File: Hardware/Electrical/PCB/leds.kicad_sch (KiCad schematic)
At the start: 0 parts

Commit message: battery charger added
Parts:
- added U7: TMP1075DSG, Package_SON:WSON-8-1EP_2x2mm_P0.5mm_EP0.9x1.6mm, symbol Sensor_Temperature:TMP1075DSG
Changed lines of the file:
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@@
 	(generator_version "9.0")
 	(paper "A4")
+	(symbol
+		(lib_id "Sensor_Temperature:TMP1075DSG")
+		(at 224.79 101.6 0)
+		(unit 1)
+		(exclude_from_sim no)
+		(in_bom yes)
+		(on_board yes)
+		(dnp no)
+		(fields_autoplaced yes)
+		(property "Reference" "U7"
+			(at 226.9333 91.44 0)
+			(effects
+				(font
+					(size 1.27 1.27)
+				)
+				(justify left)
+			)
+		)
+		(property "Value" "TMP1075DSG"
+			(at 226.9333 93.98 0)
+			(effects
+				(font
+					(size 1.27 1.27)
+				)
+				(justify left)
+			)
+		)
+		(property "Footprint" "Package_SON:WSON-8-1EP_2x2mm_P0.5mm_EP0.9x1.6mm"
+			(at 226.695 107.95 0)
+			(effects
+				(font
+					(size 1.27 1.27)
+				)
+				(hide yes)
+			)
+		)
+		(property "Datasheet" "https://www.ti.com/lit/gpn/tmp1075"
+			(at 224.79 101.6 0)
+			(effects
+				(font
+					(size 1.27 1.27)
+				)
+				(hide yes)
+			)
+		)
+		(property "Description" "I2C-bus digital temperature sensor and thermal watchdog, WSON-8"
+			(at 224.79 101.6 0)
+			(effects
+				(font
+					(size 1.27 1.27)
+				)
+				(hide yes)
+			)
+		)
+		(pin "3"
+		)
+		(pin "5"
+		)
+		(pin "6"
+		)
+		(pin "9"
+		)
+		(pin "2"
+		)
+		(pin "8"
+		)
+		(pin "1"
+		)
+		(pin "4"
+		)
+		(pin "7"
+		)
+		(instances
+			(project ""
+				(path "/8e3abcc5-43e9-4b34-9640-a0acd90473e7/255c8fde-d8cc-4a06-ba23-cdcfa512cf28"
+					(reference "U7")
+					(unit 1)
+				)
+			)
+		)
+	)
 )

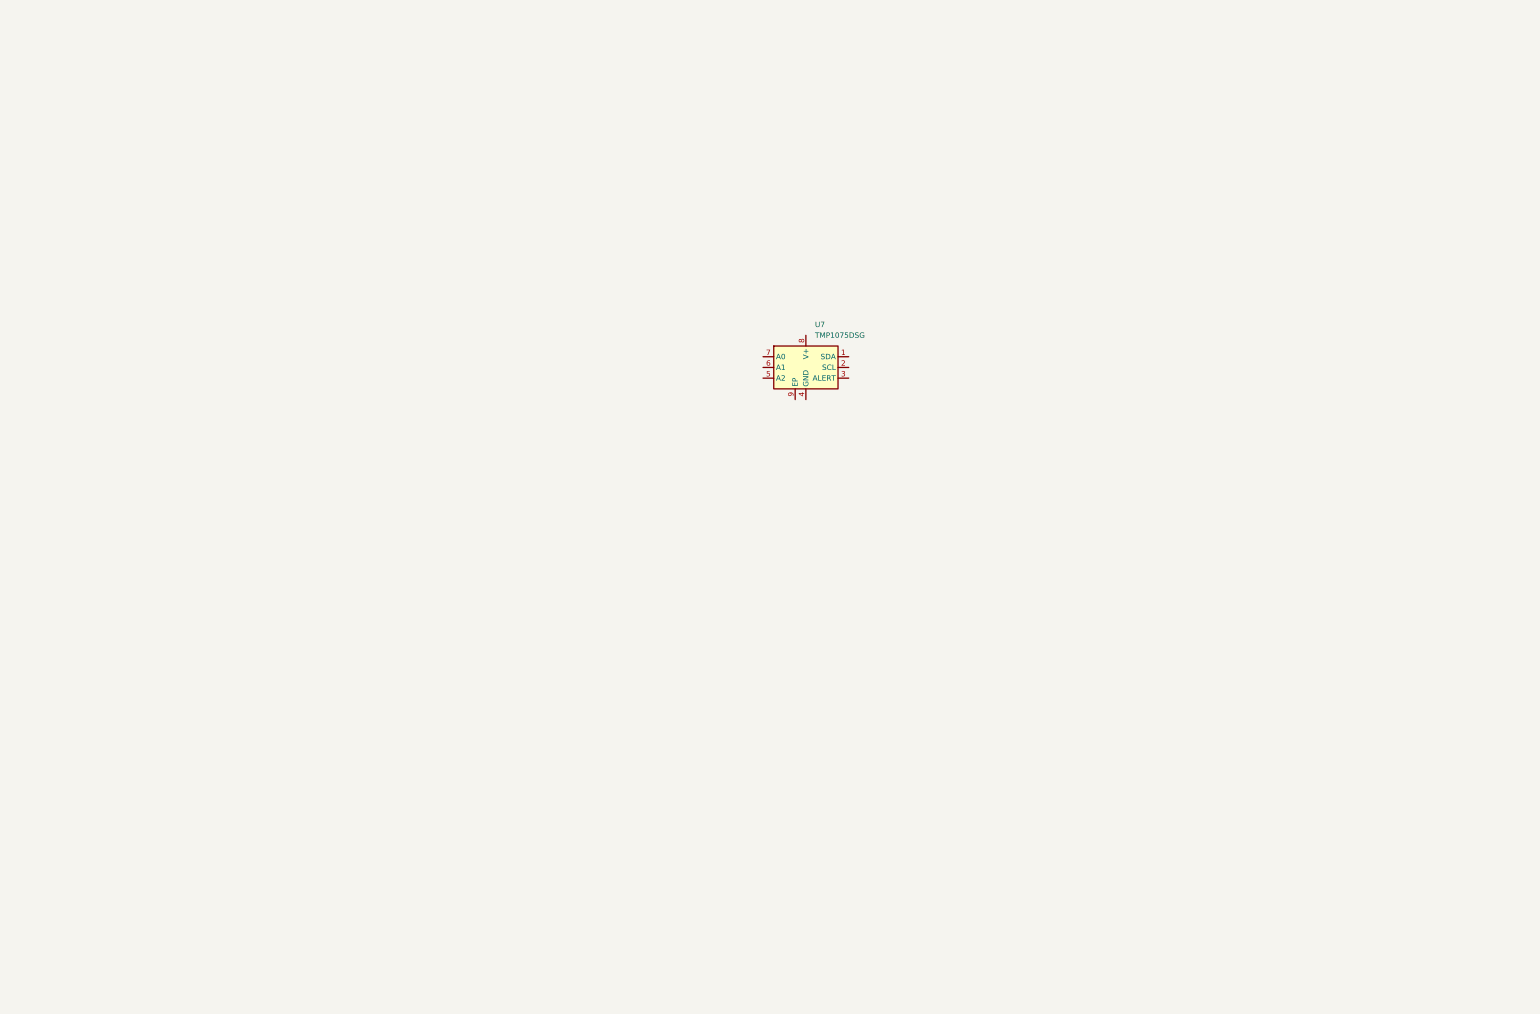
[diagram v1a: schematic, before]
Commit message: Basic Schematic finished, external connectors missing, no footprints or LCSC numbers yet
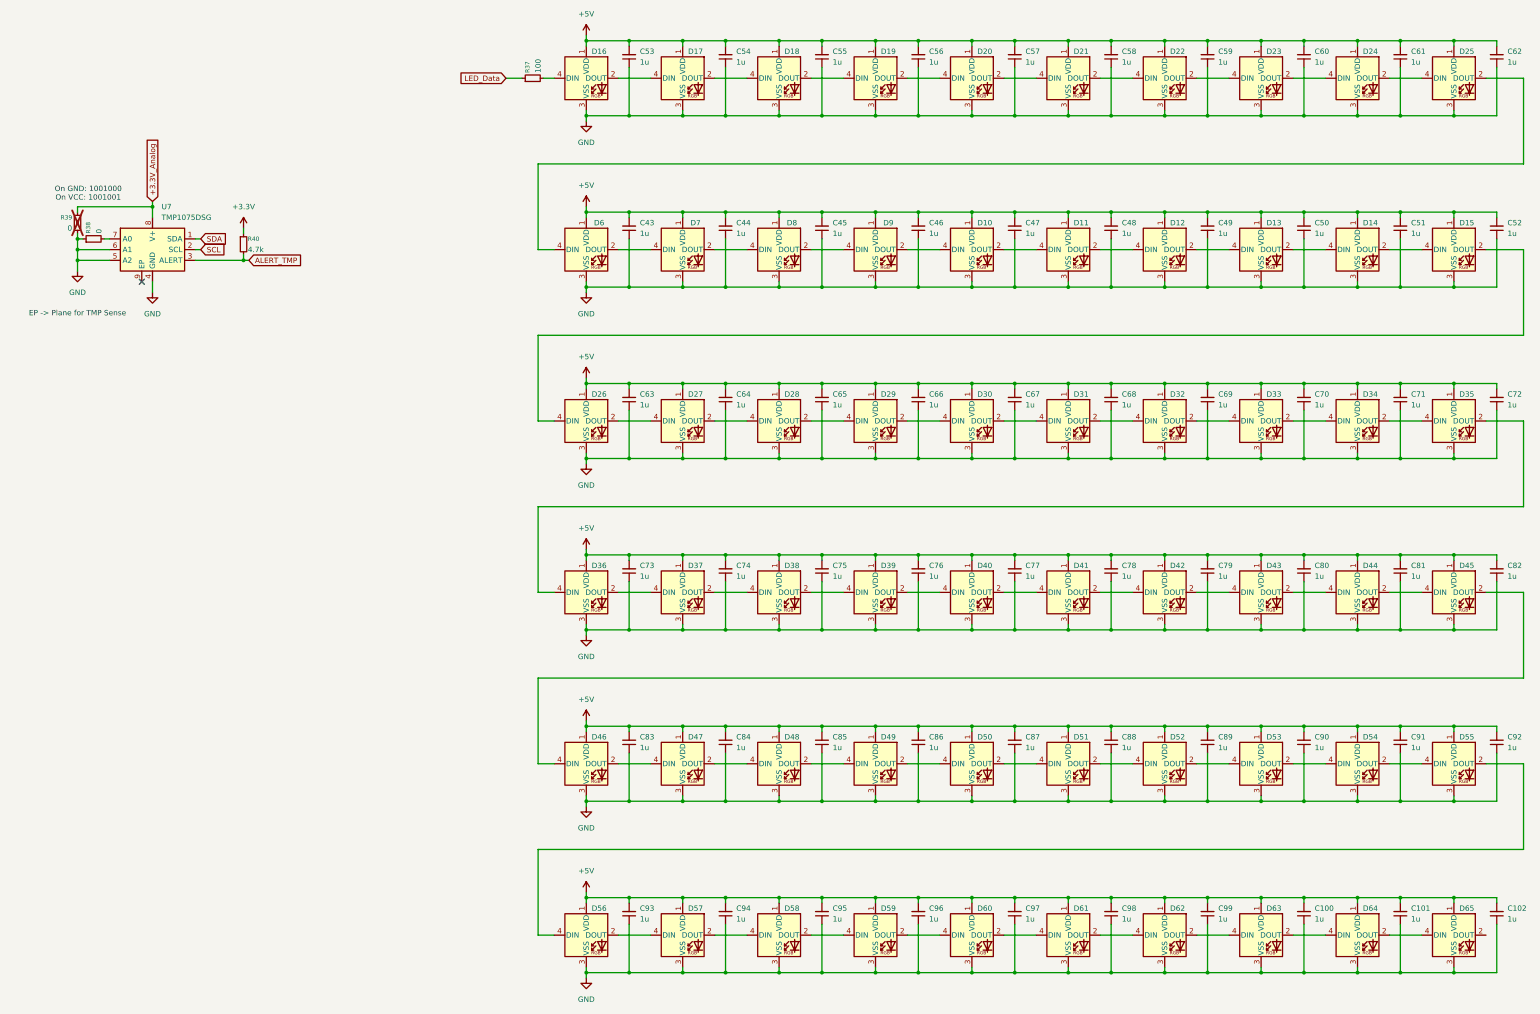
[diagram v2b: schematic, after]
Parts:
- added C100, C101, C102, C43, C44, C45, C46, C47, C48, C49, C50, C51, C52, C53, C54, C55, C56, C57, C58, C59, C60, C61, C62, C63, C64, C65, C66, C67, C68, C69, C70, C71, C72, C73, C74, C75, C76, C77, C78, C79, C80, C81, C82, C83, C84, C85, C86, C87, C88, C89, C90, C91, C92, C93, C94, C95, C96, C97, C98, C99: 1u, symbol Device:C_Small
- added D10, D11, D12, D13, D14, D15, D16, D17, D18, D19, D20, D21, D22, D23, D24, D25, D26, D27, D28, D29, D30, D31, D32, D33, D34, D35, D36, D37, D38, D39, D40, D41, D42, D43, D44, D45, D46, D47, D48, D49, D50, D51, D52, D53, D54, D55, D56, D57, D58, D59, D6, D60, D61, D62, D63, D64, D65, D7, D8, D9: WS2812B, LED_SMD:LED_WS2812B_PLCC4_5.0x5.0mm_P3.2mm, symbol LED:WS2812B
- added R37: 100, symbol Device:R_Small
- added R38, R39: 0, symbol Device:R_Small
- added R40: 4.7k, symbol Device:R_Small
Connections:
- net SDA: now reaches U7.1 (SDA)
- net SCL: now reaches U7.2 (SCL)
- net ALERT_TMP: now reaches U7.3 (ALERT)
- net ALERT_TMP: now also R40.2
- net GND: now reaches U7.4 (GND)
- net GND: now also U7.5 (A2), U7.6 (A1), C100.1, C101.1, C102.1, C43.1, C44.1, C45.1, C46.1, C47.1, C48.1, C49.1, C50.1, C51.1, C52.1, C53.1, C54.1, C55.1, C56.1, C57.1, C58.1, C59.1, C60.1, C61.1, C62.1, C63.1, C64.1, C65.1, C66.1, C67.1, C68.1, C69.1, C70.1, C71.1, C72.1, C73.1, C74.1, C75.1, C76.1, C77.1, C78.1, C79.1, C80.1, C81.1, C82.1, C83.1, C84.1, C85.1, C86.1, C87.1, C88.1, C89.1, C90.1, C91.1, C92.1, C93.1, C94.1, C95.1, C96.1, C97.1, C98.1, C99.1, D10.3 (VSS), D11.3 (VSS), D12.3 (VSS), D13.3 (VSS), D14.3 (VSS), D15.3 (VSS), D16.3 (VSS), D17.3 (VSS), D18.3 (VSS), D19.3 (VSS), D20.3 (VSS), D21.3 (VSS), D22.3 (VSS), D23.3 (VSS), D24.3 (VSS), D25.3 (VSS), D26.3 (VSS), D27.3 (VSS), D28.3 (VSS), D29.3 (VSS), D30.3 (VSS), D31.3 (VSS), D32.3 (VSS), D33.3 (VSS), D34.3 (VSS), D35.3 (VSS), D36.3 (VSS), D37.3 (VSS), D38.3 (VSS), D39.3 (VSS), D40.3 (VSS), D41.3 (VSS), D42.3 (VSS), D43.3 (VSS), D44.3 (VSS), D45.3 (VSS), D46.3 (VSS), D47.3 (VSS), D48.3 (VSS), D49.3 (VSS), D50.3 (VSS), D51.3 (VSS), D52.3 (VSS), D53.3 (VSS), D54.3 (VSS), D55.3 (VSS), D56.3 (VSS), D57.3 (VSS), D58.3 (VSS), D59.3 (VSS), D6.3 (VSS), D60.3 (VSS), D61.3 (VSS), D62.3 (VSS), D63.3 (VSS), D64.3 (VSS), D65.3 (VSS), D7.3 (VSS), D8.3 (VSS), D9.3 (VSS), R38.1, R39.2
- net at U7.7 (A0): now also R38.2
- net +3.3V_Analog: now reaches U7.8 (V+)
- net +3.3V_Analog: now also R39.1
- new net: D49.2 (DOUT), D50.4 (DIN)
- new net: D48.2 (DOUT), D49.4 (DIN)
- new net: D51.2 (DOUT), D52.4 (DIN)
- new net: D50.2 (DOUT), D51.4 (DIN)
- new net: D64.2 (DOUT), D65.4 (DIN)
- new net: D63.2 (DOUT), D64.4 (DIN)
- new net: D42.2 (DOUT), D43.4 (DIN)
- new net: D41.2 (DOUT), D42.4 (DIN)
- new net: D12.2 (DOUT), D13.4 (DIN)
- new net: D11.2 (DOUT), D12.4 (DIN)
- new net: D36.2 (DOUT), D37.4 (DIN)
- new net: D35.2 (DOUT), D36.4 (DIN)
- new net: D24.2 (DOUT), D25.4 (DIN)
- new net: D23.2 (DOUT), D24.4 (DIN)
- new net: D55.2 (DOUT), D56.4 (DIN)
- new net: D54.2 (DOUT), D55.4 (DIN)
- new net: D34.2 (DOUT), D35.4 (DIN)
- new net: D33.2 (DOUT), D34.4 (DIN)
- new net: D22.2 (DOUT), D23.4 (DIN)
- new net: D21.2 (DOUT), D22.4 (DIN)
- new net: D29.2 (DOUT), D30.4 (DIN)
- new net: D28.2 (DOUT), D29.4 (DIN)
- new net: D32.2 (DOUT), D33.4 (DIN)
- new net: D26.2 (DOUT), D27.4 (DIN)
- new net: D15.2 (DOUT), D26.4 (DIN)
- new net: D38.2 (DOUT), D39.4 (DIN)
- new net: D37.2 (DOUT), D38.4 (DIN)
- new net: D56.2 (DOUT), D57.4 (DIN)
- new net: D60.2 (DOUT), D61.4 (DIN)
- new net: D59.2 (DOUT), D60.4 (DIN)
- new net: D57.2 (DOUT), D58.4 (DIN)
- new net: D10.4 (DIN), D9.2 (DOUT)
- new net: D8.2 (DOUT), D9.4 (DIN)
- new net: D44.2 (DOUT), D45.4 (DIN)
- new net: D43.2 (DOUT), D44.4 (DIN)
- new net: D14.2 (DOUT), D15.4 (DIN)
- new net: D7.2 (DOUT), D8.4 (DIN)
- new net: D20.2 (DOUT), D21.4 (DIN)
- new net: D19.2 (DOUT), D20.4 (DIN)
- new net: D62.2 (DOUT), D63.4 (DIN)
- new net: D52.2 (DOUT), D53.4 (DIN)
- new net: D58.2 (DOUT), D59.4 (DIN)
- new net: D61.2 (DOUT), D62.4 (DIN)
- new net: D10.2 (DOUT), D11.4 (DIN)
- new net: D53.2 (DOUT), D54.4 (DIN)
- new net: D6.2 (DOUT), D7.4 (DIN)
- new net: D25.2 (DOUT), D6.4 (DIN)
- new net: D18.2 (DOUT), D19.4 (DIN)
- new net: D27.2 (DOUT), D28.4 (DIN)
- new net: D13.2 (DOUT), D14.4 (DIN)
- new net: D31.2 (DOUT), D32.4 (DIN)
- new net: D30.2 (DOUT), D31.4 (DIN)
- new net: D46.2 (DOUT), D47.4 (DIN)
- new net: D45.2 (DOUT), D46.4 (DIN)
- new net: D16.4 (DIN), R37.2
- new net: D40.2 (DOUT), D41.4 (DIN)
- new net: D47.2 (DOUT), D48.4 (DIN)
- new net: D39.2 (DOUT), D40.4 (DIN)
- new net: D16.2 (DOUT), D17.4 (DIN)
- new net: D17.2 (DOUT), D18.4 (DIN)
- new net +3.3V: R40.1
- new net +5V: C100.2, C101.2, C102.2, C43.2, C44.2, C45.2, C46.2, C47.2, C48.2, C49.2, C50.2, C51.2, C52.2, C53.2, C54.2, C55.2, C56.2, C57.2, C58.2, C59.2, C60.2, C61.2, C62.2, C63.2, C64.2, C65.2, C66.2, C67.2, C68.2, C69.2, C70.2, C71.2, C72.2, C73.2, C74.2, C75.2, C76.2, C77.2, C78.2, C79.2, C80.2, C81.2, C82.2, C83.2, C84.2, C85.2, C86.2, C87.2, C88.2, C89.2, C90.2, C91.2, C92.2, C93.2, C94.2, C95.2, C96.2, C97.2, C98.2, C99.2, D10.1 (VDD), D11.1 (VDD), D12.1 (VDD), D13.1 (VDD), D14.1 (VDD), D15.1 (VDD), D16.1 (VDD), D17.1 (VDD), D18.1 (VDD), D19.1 (VDD), D20.1 (VDD), D21.1 (VDD), D22.1 (VDD), D23.1 (VDD), D24.1 (VDD), D25.1 (VDD), D26.1 (VDD), D27.1 (VDD), D28.1 (VDD), D29.1 (VDD), D30.1 (VDD), D31.1 (VDD), D32.1 (VDD), D33.1 (VDD), D34.1 (VDD), D35.1 (VDD), D36.1 (VDD), D37.1 (VDD), D38.1 (VDD), D39.1 (VDD), D40.1 (VDD), D41.1 (VDD), D42.1 (VDD), D43.1 (VDD), D44.1 (VDD), D45.1 (VDD), D46.1 (VDD), D47.1 (VDD), D48.1 (VDD), D49.1 (VDD), D50.1 (VDD), D51.1 (VDD), D52.1 (VDD), D53.1 (VDD), D54.1 (VDD), D55.1 (VDD), D56.1 (VDD), D57.1 (VDD), D58.1 (VDD), D59.1 (VDD), D6.1 (VDD), D60.1 (VDD), D61.1 (VDD), D62.1 (VDD), D63.1 (VDD), D64.1 (VDD), D65.1 (VDD), D7.1 (VDD), D8.1 (VDD), D9.1 (VDD)
- new net LED_Data: R37.1
- no-connect marks 0 -> 1
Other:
- note added: "EP -> Plane for TMP Sense"
- note added: "On GND: 1001000 On VCC: 1001001"
- moved on the sheet: U7

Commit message: layout v1 finished but not confirmed yet
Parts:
- C100: renamed from C102; footprint (none) -> Capacitor_SMD:C_0603_1608Metric; *LCSC Part Number (none) -> C1848
- C13: renamed from C53; footprint (none) -> Capacitor_SMD:C_0603_1608Metric; *LCSC Part Number (none) -> C1848
- C15: renamed from C54; footprint (none) -> Capacitor_SMD:C_0603_1608Metric; *LCSC Part Number (none) -> C1848
- C43: renamed from C55; footprint (none) -> Capacitor_SMD:C_0603_1608Metric; *LCSC Part Number (none) -> C1848
- C44: renamed from C56; footprint (none) -> Capacitor_SMD:C_0603_1608Metric; *LCSC Part Number (none) -> C1848
- C45: renamed from C57; footprint (none) -> Capacitor_SMD:C_0603_1608Metric; *LCSC Part Number (none) -> C1848
- C46: renamed from C58; footprint (none) -> Capacitor_SMD:C_0603_1608Metric; *LCSC Part Number (none) -> C1848
- C47: renamed from C59; footprint (none) -> Capacitor_SMD:C_0603_1608Metric; *LCSC Part Number (none) -> C1848
- C48: renamed from C60; footprint (none) -> Capacitor_SMD:C_0603_1608Metric; *LCSC Part Number (none) -> C1848
- C49: renamed from C61; footprint (none) -> Capacitor_SMD:C_0603_1608Metric; *LCSC Part Number (none) -> C1848
- C50: renamed from C62; footprint (none) -> Capacitor_SMD:C_0603_1608Metric; *LCSC Part Number (none) -> C1848
- C51: renamed from C43; footprint (none) -> Capacitor_SMD:C_0603_1608Metric; *LCSC Part Number (none) -> C1848
- C52: renamed from C44; footprint (none) -> Capacitor_SMD:C_0603_1608Metric; *LCSC Part Number (none) -> C1848
- C53: renamed from C45; footprint (none) -> Capacitor_SMD:C_0603_1608Metric; *LCSC Part Number (none) -> C1848
- C54: renamed from C46; footprint (none) -> Capacitor_SMD:C_0603_1608Metric; *LCSC Part Number (none) -> C1848
- C55: renamed from C47; footprint (none) -> Capacitor_SMD:C_0603_1608Metric; *LCSC Part Number (none) -> C1848
- C56: renamed from C48; footprint (none) -> Capacitor_SMD:C_0603_1608Metric; *LCSC Part Number (none) -> C1848
- C57: renamed from C49; footprint (none) -> Capacitor_SMD:C_0603_1608Metric; *LCSC Part Number (none) -> C1848
- C58: renamed from C50; footprint (none) -> Capacitor_SMD:C_0603_1608Metric; *LCSC Part Number (none) -> C1848
- C59: renamed from C51; footprint (none) -> Capacitor_SMD:C_0603_1608Metric; *LCSC Part Number (none) -> C1848
- C60: renamed from C52; footprint (none) -> Capacitor_SMD:C_0603_1608Metric; *LCSC Part Number (none) -> C1848
- C61: renamed from C63; footprint (none) -> Capacitor_SMD:C_0603_1608Metric; *LCSC Part Number (none) -> C1848
- C62: renamed from C64; footprint (none) -> Capacitor_SMD:C_0603_1608Metric; *LCSC Part Number (none) -> C1848
- C63: renamed from C65; footprint (none) -> Capacitor_SMD:C_0603_1608Metric; *LCSC Part Number (none) -> C1848
- C64: renamed from C66; footprint (none) -> Capacitor_SMD:C_0603_1608Metric; *LCSC Part Number (none) -> C1848
- C65: renamed from C67; footprint (none) -> Capacitor_SMD:C_0603_1608Metric; *LCSC Part Number (none) -> C1848
- C66: renamed from C68; footprint (none) -> Capacitor_SMD:C_0603_1608Metric; *LCSC Part Number (none) -> C1848
- C67: renamed from C69; footprint (none) -> Capacitor_SMD:C_0603_1608Metric; *LCSC Part Number (none) -> C1848
- C68: renamed from C70; footprint (none) -> Capacitor_SMD:C_0603_1608Metric; *LCSC Part Number (none) -> C1848
- C69: renamed from C71; footprint (none) -> Capacitor_SMD:C_0603_1608Metric; *LCSC Part Number (none) -> C1848
- C70: renamed from C72; footprint (none) -> Capacitor_SMD:C_0603_1608Metric; *LCSC Part Number (none) -> C1848
- C71: renamed from C73; footprint (none) -> Capacitor_SMD:C_0603_1608Metric; *LCSC Part Number (none) -> C1848
- C72: renamed from C74; footprint (none) -> Capacitor_SMD:C_0603_1608Metric; *LCSC Part Number (none) -> C1848
- C73: renamed from C75; footprint (none) -> Capacitor_SMD:C_0603_1608Metric; *LCSC Part Number (none) -> C1848
- C74: renamed from C76; footprint (none) -> Capacitor_SMD:C_0603_1608Metric; *LCSC Part Number (none) -> C1848
- C75: renamed from C77; footprint (none) -> Capacitor_SMD:C_0603_1608Metric; *LCSC Part Number (none) -> C1848
- C76: renamed from C78; footprint (none) -> Capacitor_SMD:C_0603_1608Metric; *LCSC Part Number (none) -> C1848
- C77: renamed from C79; footprint (none) -> Capacitor_SMD:C_0603_1608Metric; *LCSC Part Number (none) -> C1848
- C78: renamed from C80; footprint (none) -> Capacitor_SMD:C_0603_1608Metric; *LCSC Part Number (none) -> C1848
- C79: renamed from C81; footprint (none) -> Capacitor_SMD:C_0603_1608Metric; *LCSC Part Number (none) -> C1848
- C80: renamed from C82; footprint (none) -> Capacitor_SMD:C_0603_1608Metric; *LCSC Part Number (none) -> C1848
- C81: renamed from C83; footprint (none) -> Capacitor_SMD:C_0603_1608Metric; *LCSC Part Number (none) -> C1848
- C82: renamed from C84; footprint (none) -> Capacitor_SMD:C_0603_1608Metric; *LCSC Part Number (none) -> C1848
- C83: renamed from C85; footprint (none) -> Capacitor_SMD:C_0603_1608Metric; *LCSC Part Number (none) -> C1848
- C84: renamed from C86; footprint (none) -> Capacitor_SMD:C_0603_1608Metric; *LCSC Part Number (none) -> C1848
- C85: renamed from C87; footprint (none) -> Capacitor_SMD:C_0603_1608Metric; *LCSC Part Number (none) -> C1848
- C86: renamed from C88; footprint (none) -> Capacitor_SMD:C_0603_1608Metric; *LCSC Part Number (none) -> C1848
- C87: renamed from C89; footprint (none) -> Capacitor_SMD:C_0603_1608Metric; *LCSC Part Number (none) -> C1848
- C88: renamed from C90; footprint (none) -> Capacitor_SMD:C_0603_1608Metric; *LCSC Part Number (none) -> C1848
- C89: renamed from C91; footprint (none) -> Capacitor_SMD:C_0603_1608Metric; *LCSC Part Number (none) -> C1848
- C90: renamed from C92; footprint (none) -> Capacitor_SMD:C_0603_1608Metric; *LCSC Part Number (none) -> C1848
- C91: renamed from C93; footprint (none) -> Capacitor_SMD:C_0603_1608Metric; *LCSC Part Number (none) -> C1848
- C92: renamed from C94; footprint (none) -> Capacitor_SMD:C_0603_1608Metric; *LCSC Part Number (none) -> C1848
- C93: renamed from C95; footprint (none) -> Capacitor_SMD:C_0603_1608Metric; *LCSC Part Number (none) -> C1848
- C94: renamed from C96; footprint (none) -> Capacitor_SMD:C_0603_1608Metric; *LCSC Part Number (none) -> C1848
- C95: renamed from C97; footprint (none) -> Capacitor_SMD:C_0603_1608Metric; *LCSC Part Number (none) -> C1848
- C96: renamed from C98; footprint (none) -> Capacitor_SMD:C_0603_1608Metric; *LCSC Part Number (none) -> C1848
- C97: renamed from C99; footprint (none) -> Capacitor_SMD:C_0603_1608Metric; *LCSC Part Number (none) -> C1848
- C98: renamed from C100; footprint (none) -> Capacitor_SMD:C_0603_1608Metric; *LCSC Part Number (none) -> C1848
- C99: renamed from C101; footprint (none) -> Capacitor_SMD:C_0603_1608Metric; *LCSC Part Number (none) -> C1848
- D10: renamed from D20; *LCSC Part Number (none) -> C114587
- D11: renamed from D21; *LCSC Part Number (none) -> C114587
- D12: renamed from D22; *LCSC Part Number (none) -> C114587
- D13: renamed from D23; *LCSC Part Number (none) -> C114587
- D14: renamed from D24; *LCSC Part Number (none) -> C114587
- D15: renamed from D25; *LCSC Part Number (none) -> C114587
- D16: renamed from D6; *LCSC Part Number (none) -> C114587
- D17: renamed from D7; *LCSC Part Number (none) -> C114587
- D18: renamed from D8; *LCSC Part Number (none) -> C114587
- D19: renamed from D9; *LCSC Part Number (none) -> C114587
- D20: renamed from D10; *LCSC Part Number (none) -> C114587
- D21: renamed from D11; *LCSC Part Number (none) -> C114587
- D22: renamed from D12; *LCSC Part Number (none) -> C114587
- D23: renamed from D13; *LCSC Part Number (none) -> C114587
- D24: renamed from D14; *LCSC Part Number (none) -> C114587
- D25: renamed from D15; *LCSC Part Number (none) -> C114587
- D26, D27, D28, D29, D30, D31, D32, D33, D34, D35, D36, D37, D38, D39, D40, D41, D42, D43, D44, D45, D46, D47, D48, D49, D50, D51, D52, D53, D54, D55, D56, D57, D58, D59, D60, D61, D62, D63, D64, D65: *LCSC Part Number (none) -> C114587
- D6: renamed from D16; *LCSC Part Number (none) -> C114587
- D7: renamed from D17; *LCSC Part Number (none) -> C114587
- D8: renamed from D18; *LCSC Part Number (none) -> C114587
- D9: renamed from D19; *LCSC Part Number (none) -> C114587
- R37: footprint (none) -> Resistor_SMD:R_0603_1608Metric; *LCSC Part Number (none) -> C22775
- R38: renamed from R39; footprint (none) -> Resistor_SMD:R_0603_1608Metric
- R39: renamed from R40; footprint (none) -> Resistor_SMD:R_0603_1608Metric; *LCSC Part Number (none) -> C23162
- R40: renamed from R38; footprint (none) -> Resistor_SMD:R_0603_1608Metric; *LCSC Part Number (none) -> C21189
- U7: *LCSC Part Number (none) -> C2870250
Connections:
- net +3.3V is gone; now on net +3.3V_Analog: R39.1
- net GND: now also R40.2; no longer R38.2, R40.1, U7.5 (A2), U7.6 (A1)
- net at U7.7 (A0): now also R38.2, R40.1, U7.5 (A2), U7.6 (A1); no longer R40.2
- no-connect marks 1 -> 2
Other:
- moved on the sheet: R40
